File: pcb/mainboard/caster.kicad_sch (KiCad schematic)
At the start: 2 parts, among them U1001 XC7A15T-FTG256, U1002 MT41K64M16HA

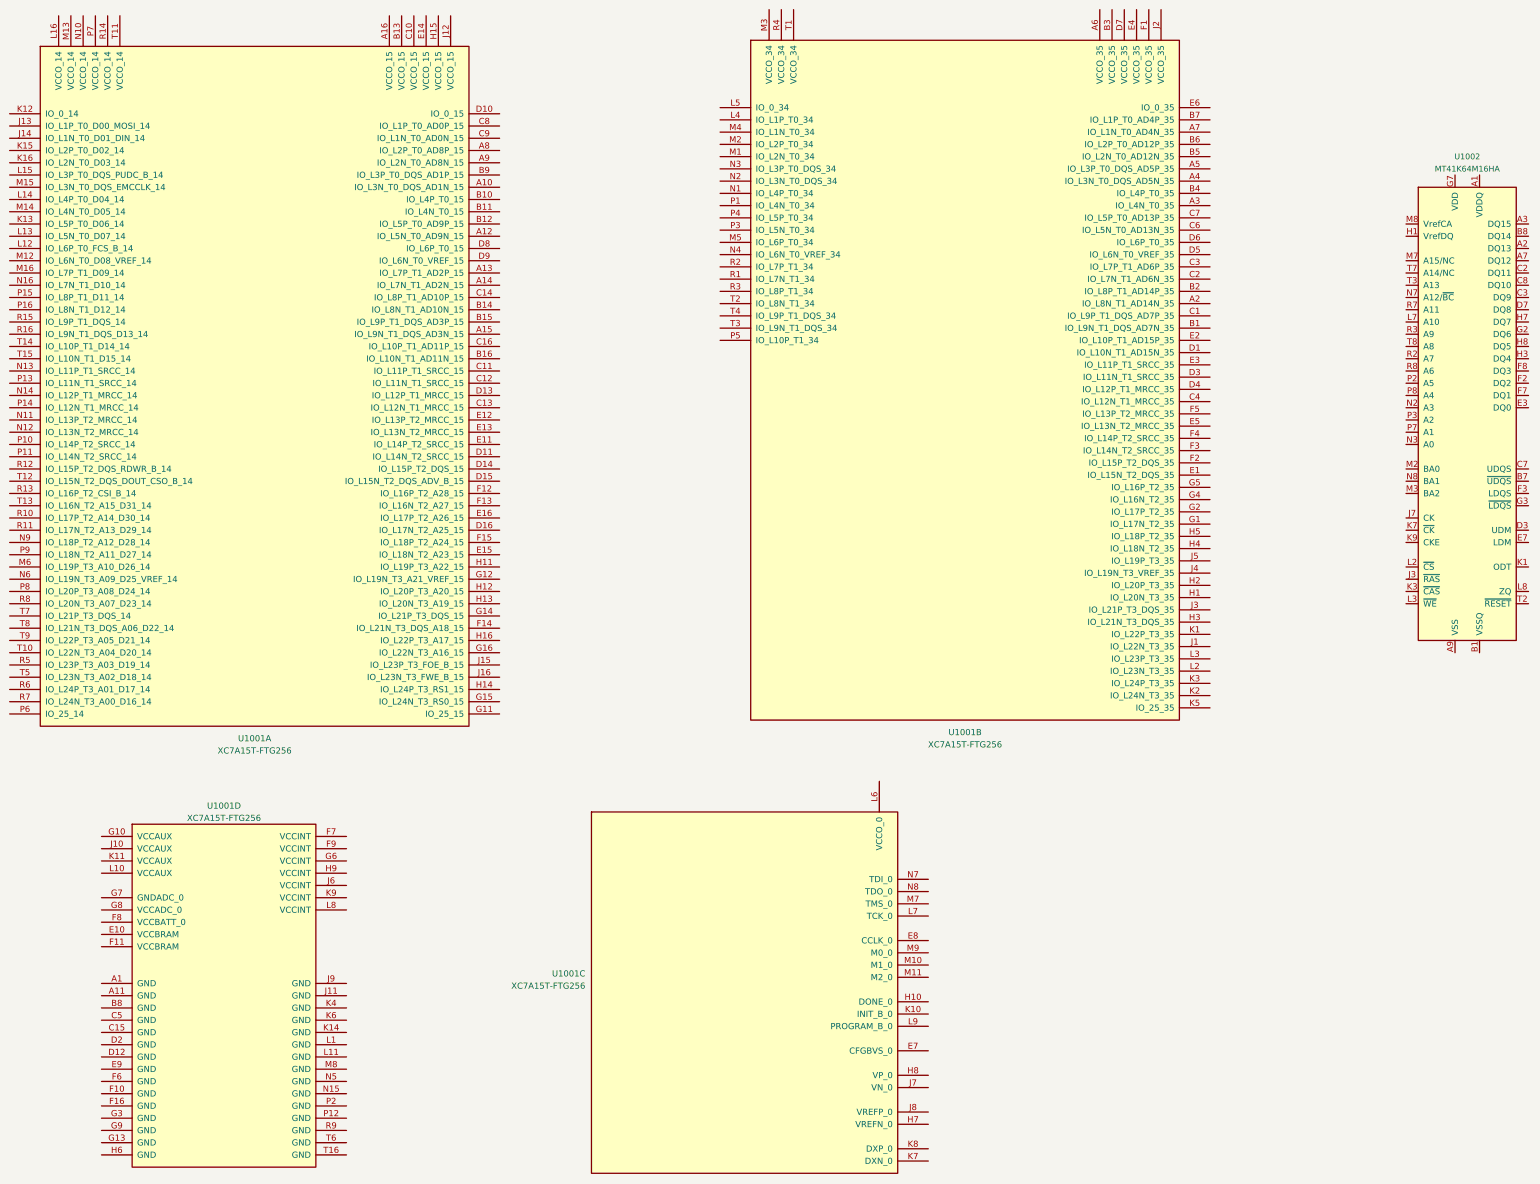
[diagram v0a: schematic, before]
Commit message: - pcb: ddr layout
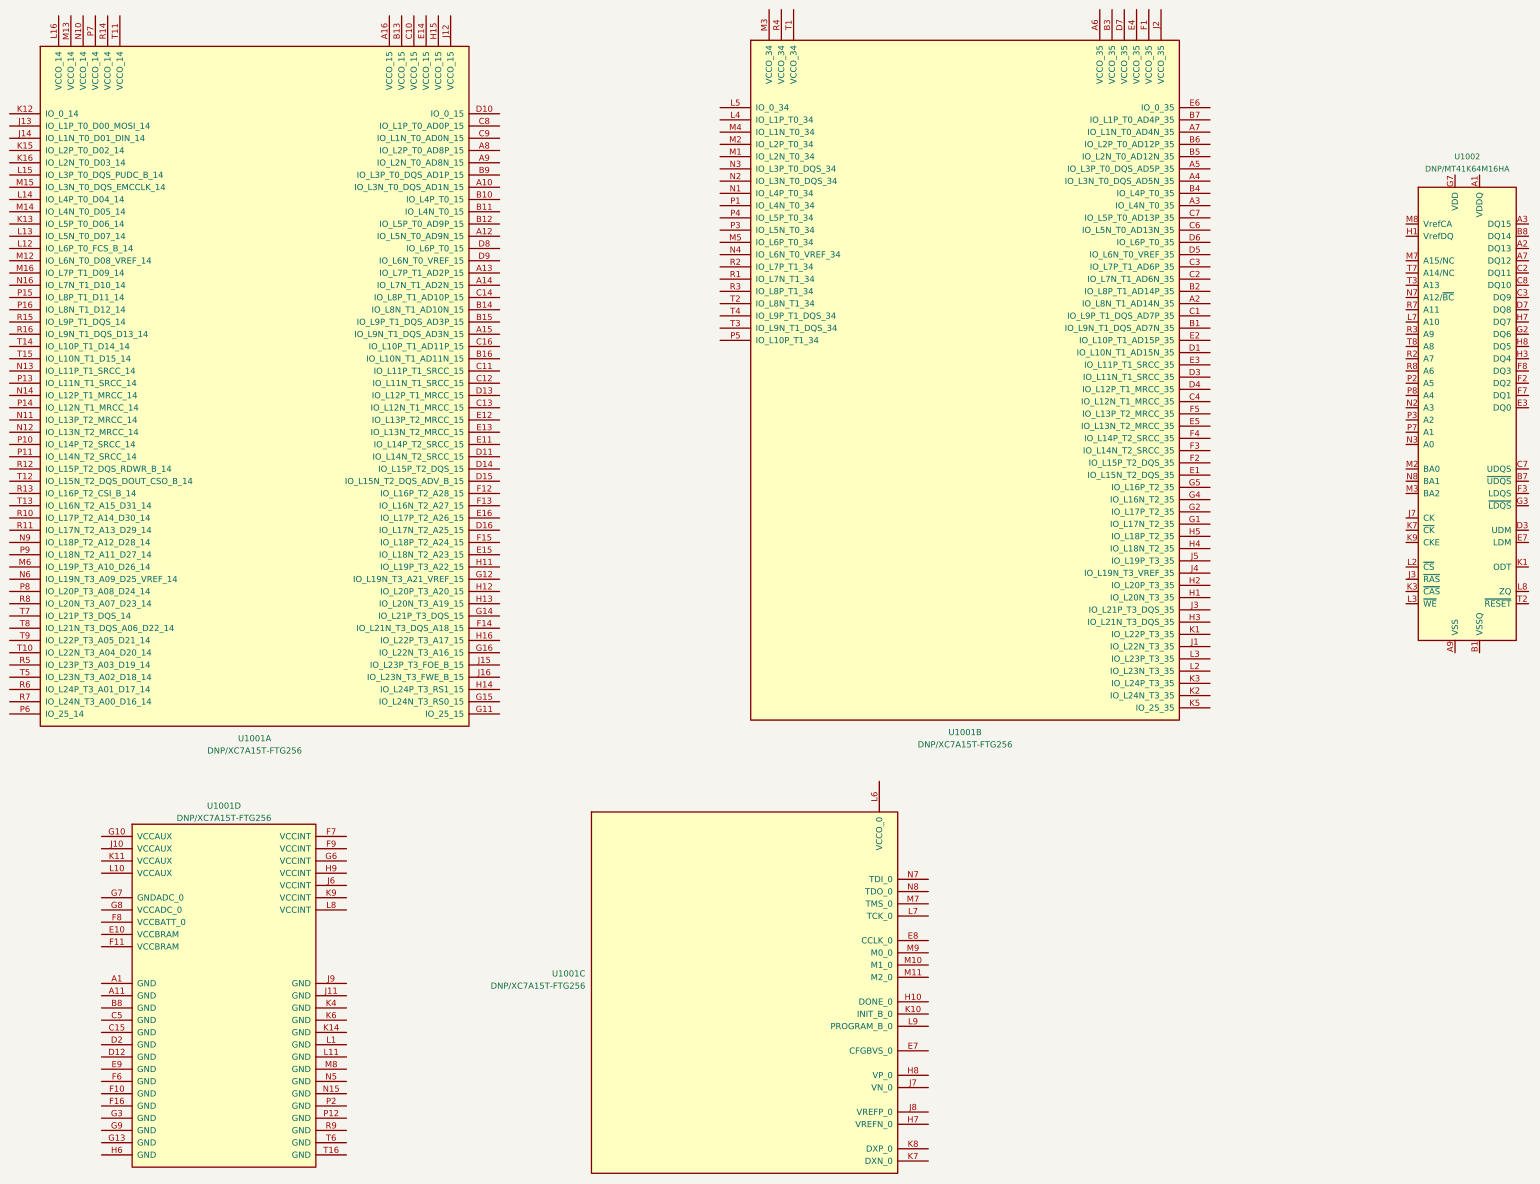
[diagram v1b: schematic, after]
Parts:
- U1001: value XC7A15T-FTG256 -> DNP/XC7A15T-FTG256; footprint (none) -> Package_BGA:Xilinx_FTG256
- U1002: value MT41K64M16HA -> DNP/MT41K64M16HA
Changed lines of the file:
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@@
       (effects (font (size 1.1938 1.1938)))
     )
-    (property "Value" "MT41K64M16HA" (id 1) (at 346.71 62.23 0)
+    (property "Value" "DNP/MT41K64M16HA" (id 1) (at 346.71 62.23 0)
       (effects (font (size 1.1938 1.1938)))
     )
@@
     (in_bom yes) (on_board yes) (fields_autoplaced)
     (property "Reference" "U1001" (id 0) (at 88.9 194.31 0))
-    (property "Value" "XC7A15T-FTG256" (id 1) (at 88.9 196.85 0))
-    (property "Footprint" "" (id 2) (at 88.9 233.68 0)
+    (property "Value" "DNP/XC7A15T-FTG256" (id 1) (at 88.9 196.85 0))
+    (property "Footprint" "Package_BGA:Xilinx_FTG256" (id 2) (at 88.9 233.68 0)
       (effects (font (size 1.27 1.27)) hide)
     )
@@
       (effects (font (size 1.27 1.27)) (justify right))
     )
-    (property "Value" "XC7A15T-FTG256" (id 1) (at 163.83 231.6479 0)
+    (property "Value" "DNP/XC7A15T-FTG256" (id 1) (at 163.83 231.6479 0)
       (effects (font (size 1.27 1.27)) (justify right))
     )
-    (property "Footprint" "" (id 2) (at 196.85 229.87 0)
+    (property "Footprint" "Package_BGA:Xilinx_FTG256" (id 2) (at 196.85 229.87 0)
       (effects (font (size 1.27 1.27)) hide)
     )
@@
     (in_bom yes) (on_board yes) (fields_autoplaced)
     (property "Reference" "U1001" (id 0) (at 95.25 180.34 0))
-    (property "Value" "XC7A15T-FTG256" (id 1) (at 95.25 182.88 0))
-    (property "Footprint" "" (id 2) (at 95.25 104.14 0)
+    (property "Value" "DNP/XC7A15T-FTG256" (id 1) (at 95.25 182.88 0))
+    (property "Footprint" "Package_BGA:Xilinx_FTG256" (id 2) (at 95.25 104.14 0)
       (effects (font (size 1.27 1.27)) hide)
     )
@@
     (in_bom yes) (on_board yes) (fields_autoplaced)
     (property "Reference" "U1001" (id 0) (at 242.57 179.07 0))
-    (property "Value" "XC7A15T-FTG256" (id 1) (at 242.57 181.61 0))
-    (property "Footprint" "" (id 2) (at 242.57 102.87 0)
+    (property "Value" "DNP/XC7A15T-FTG256" (id 1) (at 242.57 181.61 0))
+    (property "Footprint" "Package_BGA:Xilinx_FTG256" (id 2) (at 242.57 102.87 0)
       (effects (font (size 1.27 1.27)) hide)
     )

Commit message: - pcb: finishing layout r0p1
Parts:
- removed U1001: DNP/XC7A15T-FTG256, Package_BGA:Xilinx_FTG256, symbol FPGA_Xilinx_Artix7:XC7A15T-FTG256
- removed U1002: DNP/MT41K64M16HA, Package_BGA:BGA-96_9.0x13.0mm_Layout2x3x16_P0.8mm, symbol symbols:MT41K256M16HA
